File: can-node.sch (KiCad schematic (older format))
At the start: 11 parts, among them P2 CONN_01X06, Q16 IRLML0060, Q17 IRLML0060, U6 LTV-356T, U7 LTV-356T

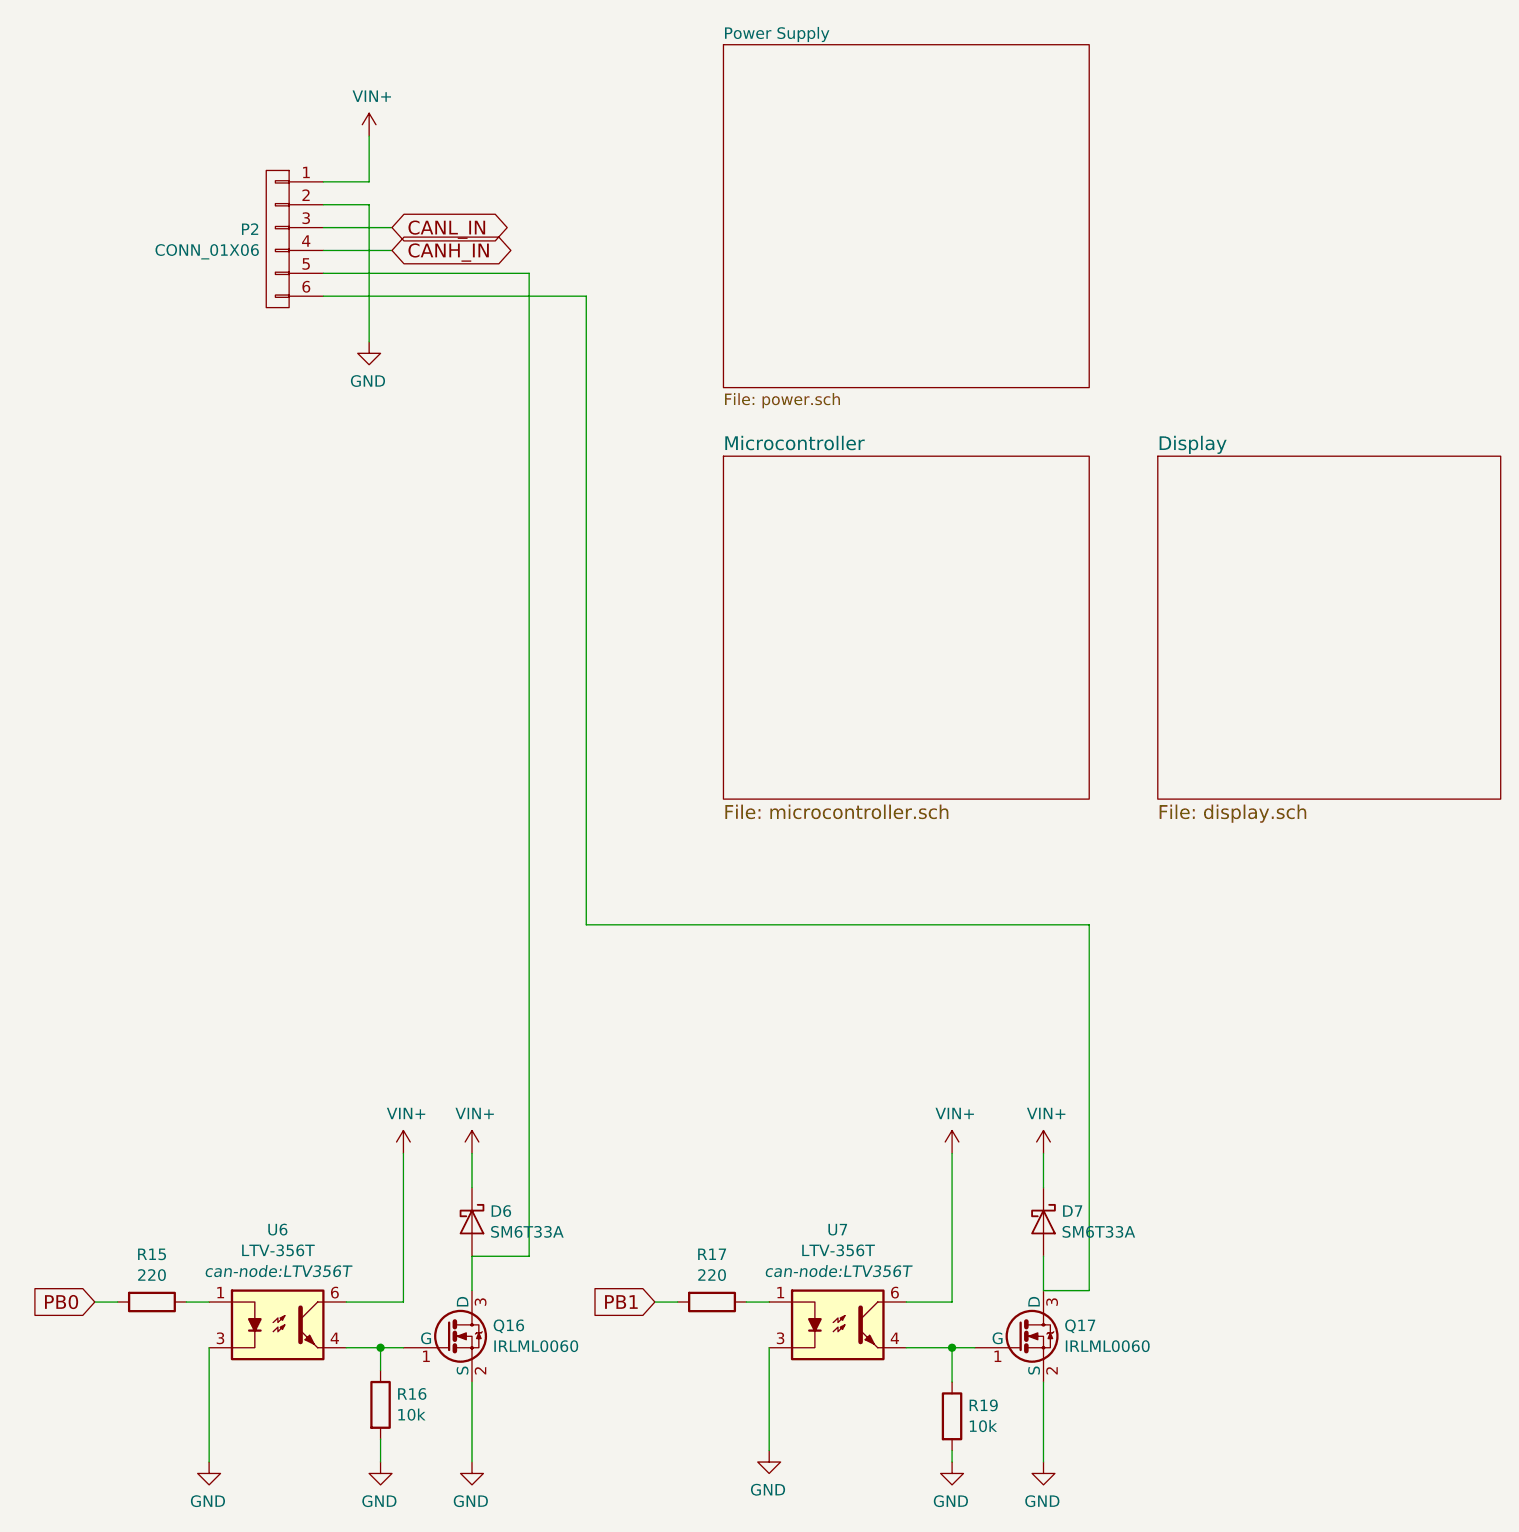
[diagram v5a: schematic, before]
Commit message: Remove unnecessary 24V out, minor changes.
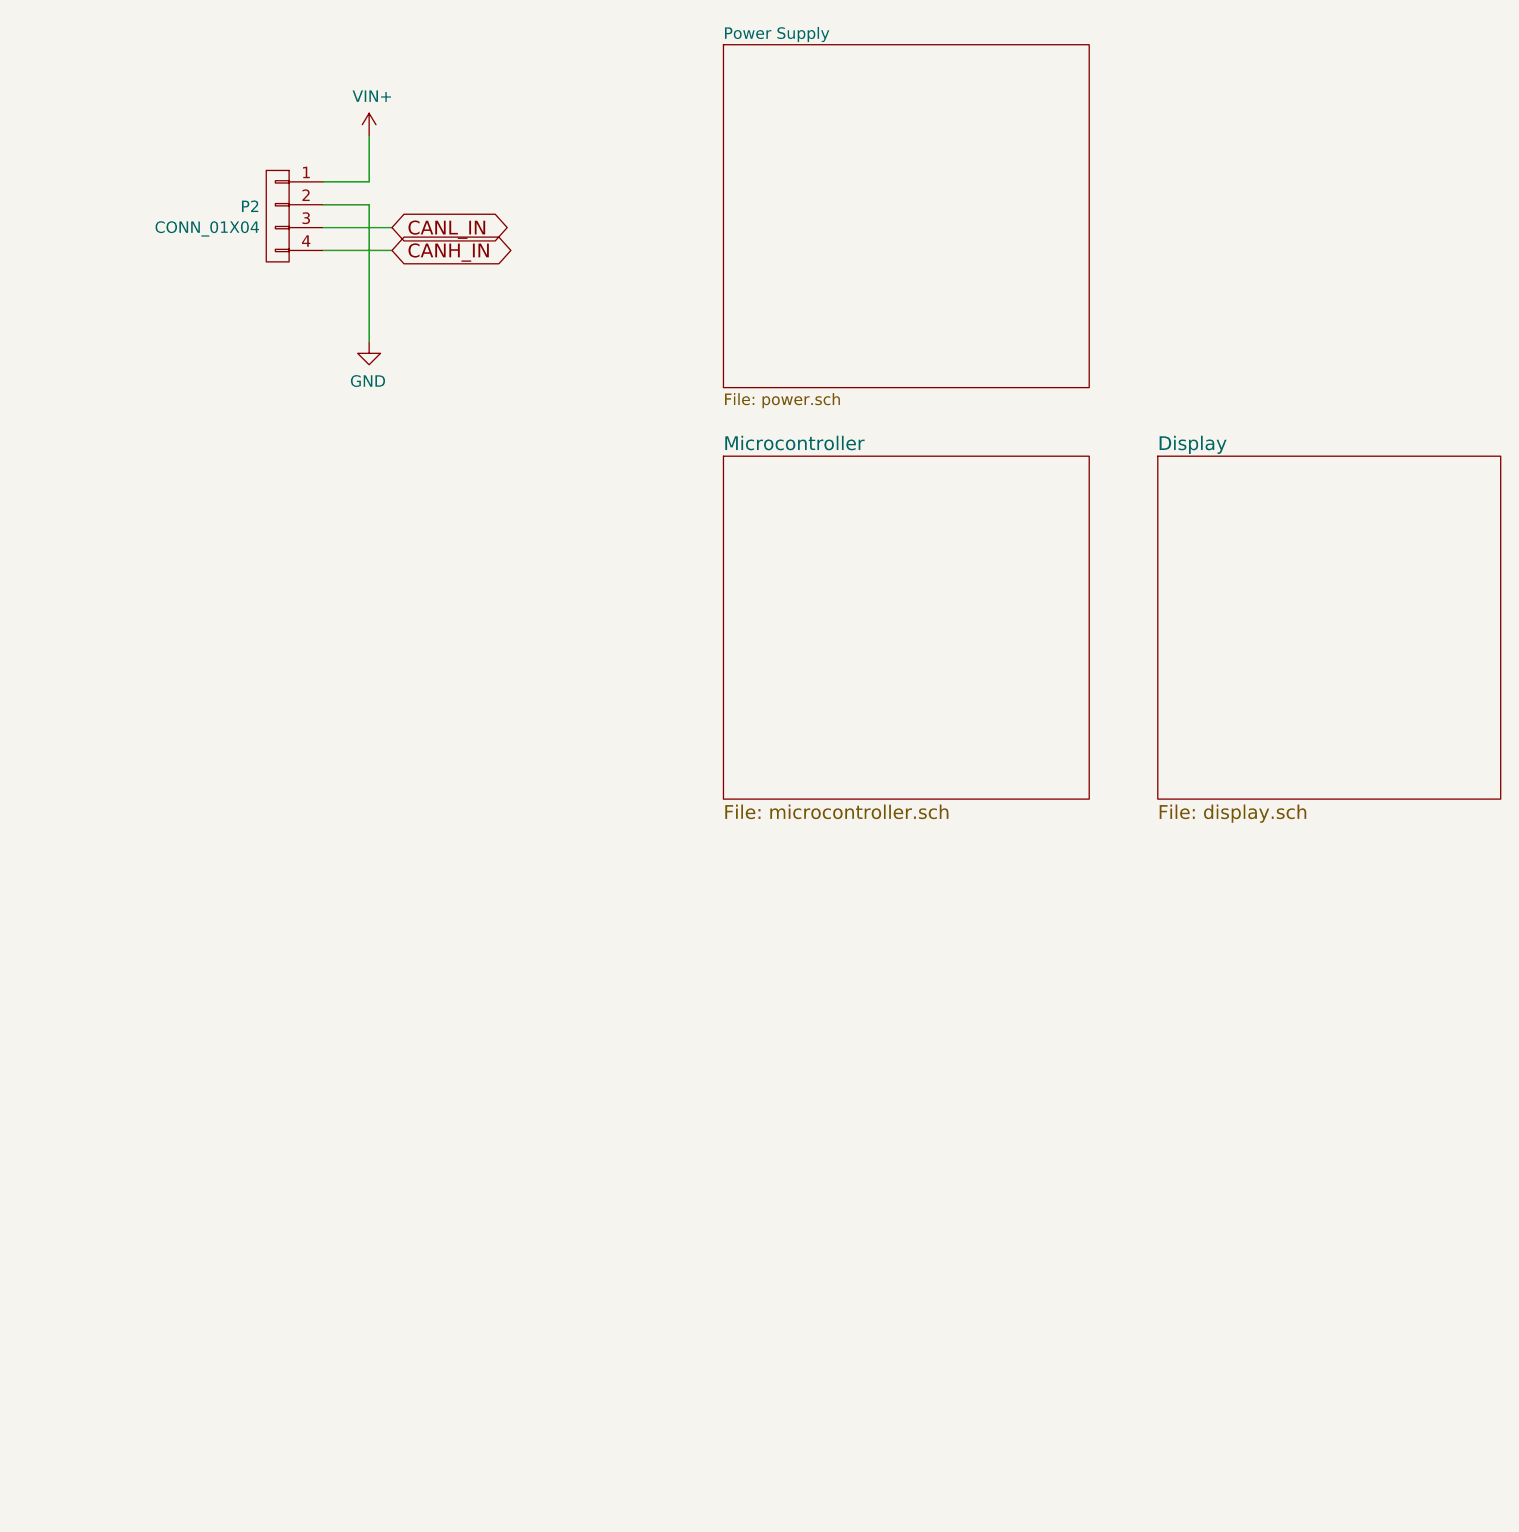
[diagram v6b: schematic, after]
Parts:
- removed D6, D7: SM6T33A, Diodes_SMD:SMB_Standard, symbol D_Schottky
- removed P2: CONN_01X06, can-node:WAGO_218-106, symbol CONN_01X06
- removed Q16, Q17: IRLML0060, TO_SOT_Packages_SMD:SOT-23, symbol IRLML0060
- removed R15, R17: 220, Resistors_SMD:R_0402, symbol R
- removed R16, R19: 10k, Resistors_SMD:R_0402, symbol R
- removed U6, U7: LTV-356T, can-node:LTV356T, symbol LTV-356T
- added P2: CONN_01X04, can-node:WAGO_218-104, symbol CONN_01X04
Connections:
- net CANH_IN: now also P2.4 (P4)
- net CANL_IN: now also P2.3 (P3)
- net GND: now also P2.2 (P2)
- net VIN+: now also P2.1 (P1)
